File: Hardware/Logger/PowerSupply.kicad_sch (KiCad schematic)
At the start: 13 parts, among them J5 USB_B_Micro, U3 LD1117ASTR

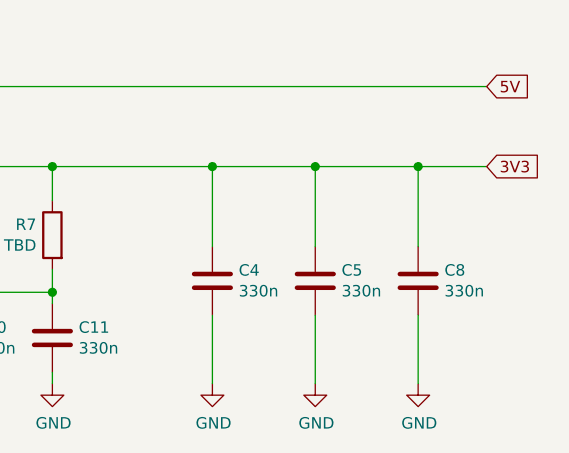
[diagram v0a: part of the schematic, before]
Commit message: draft of rev 3.0, cleanup of repo from not fully open source libs
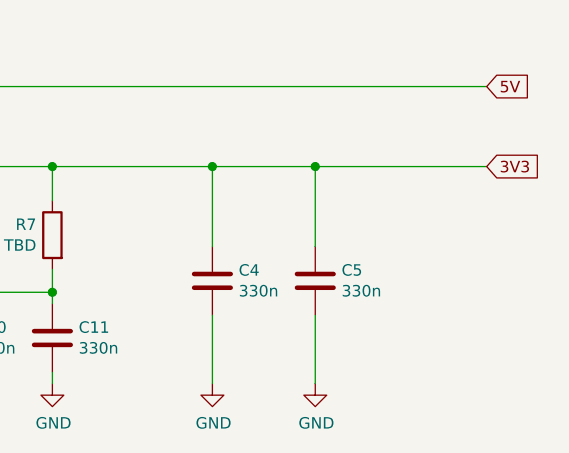
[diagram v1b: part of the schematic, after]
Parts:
- removed C8: 330n, Capacitor_SMD:C_0805_2012Metric, symbol Device:C
